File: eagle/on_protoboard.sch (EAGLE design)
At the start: 15 parts, among them IC2 7812T, K1 G6AK-434P

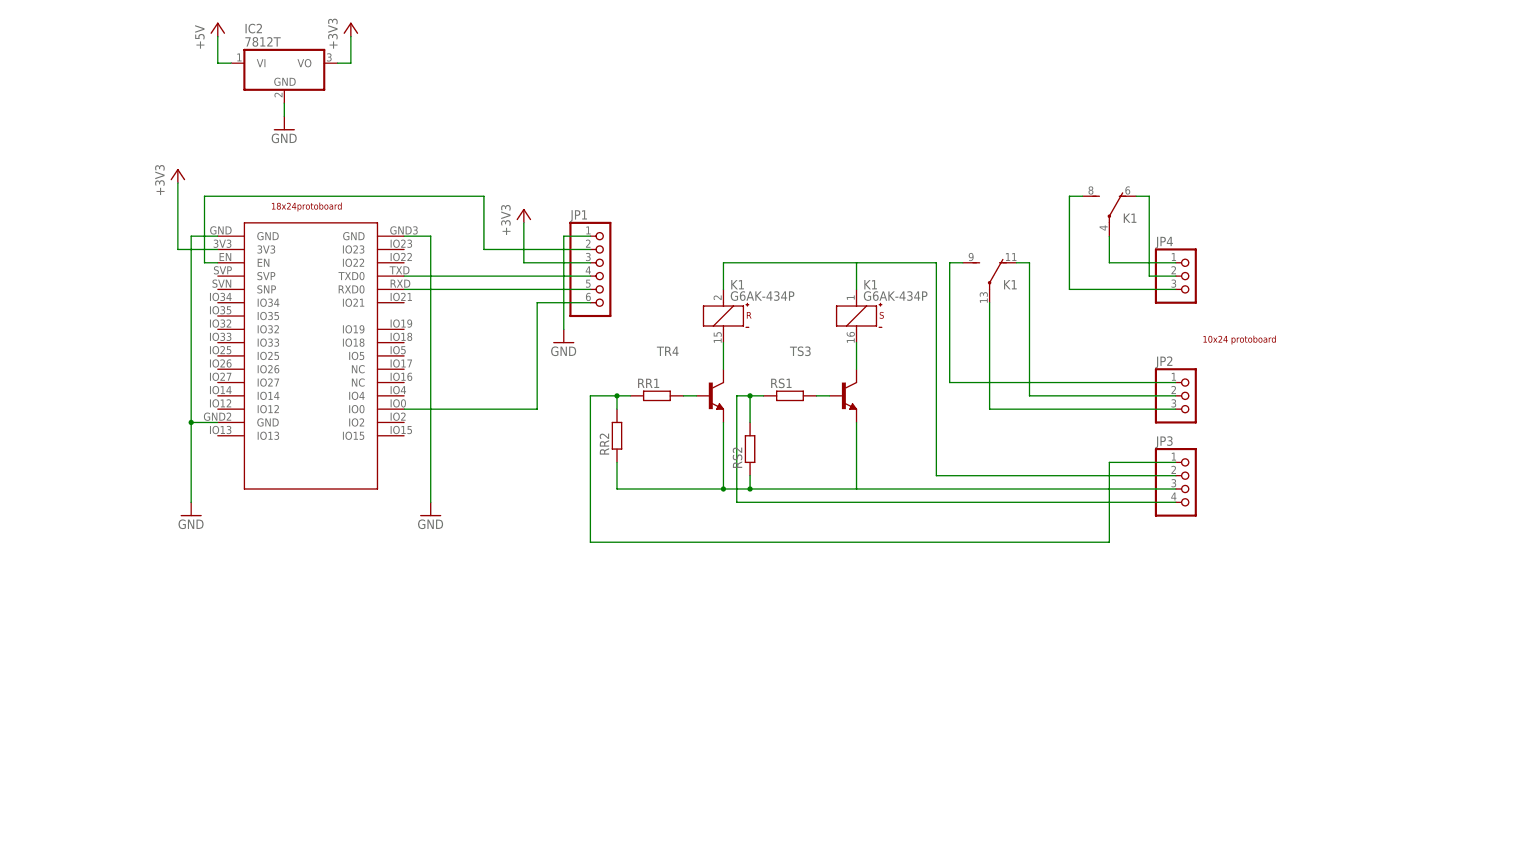
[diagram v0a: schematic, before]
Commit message: Add digital pulse output device
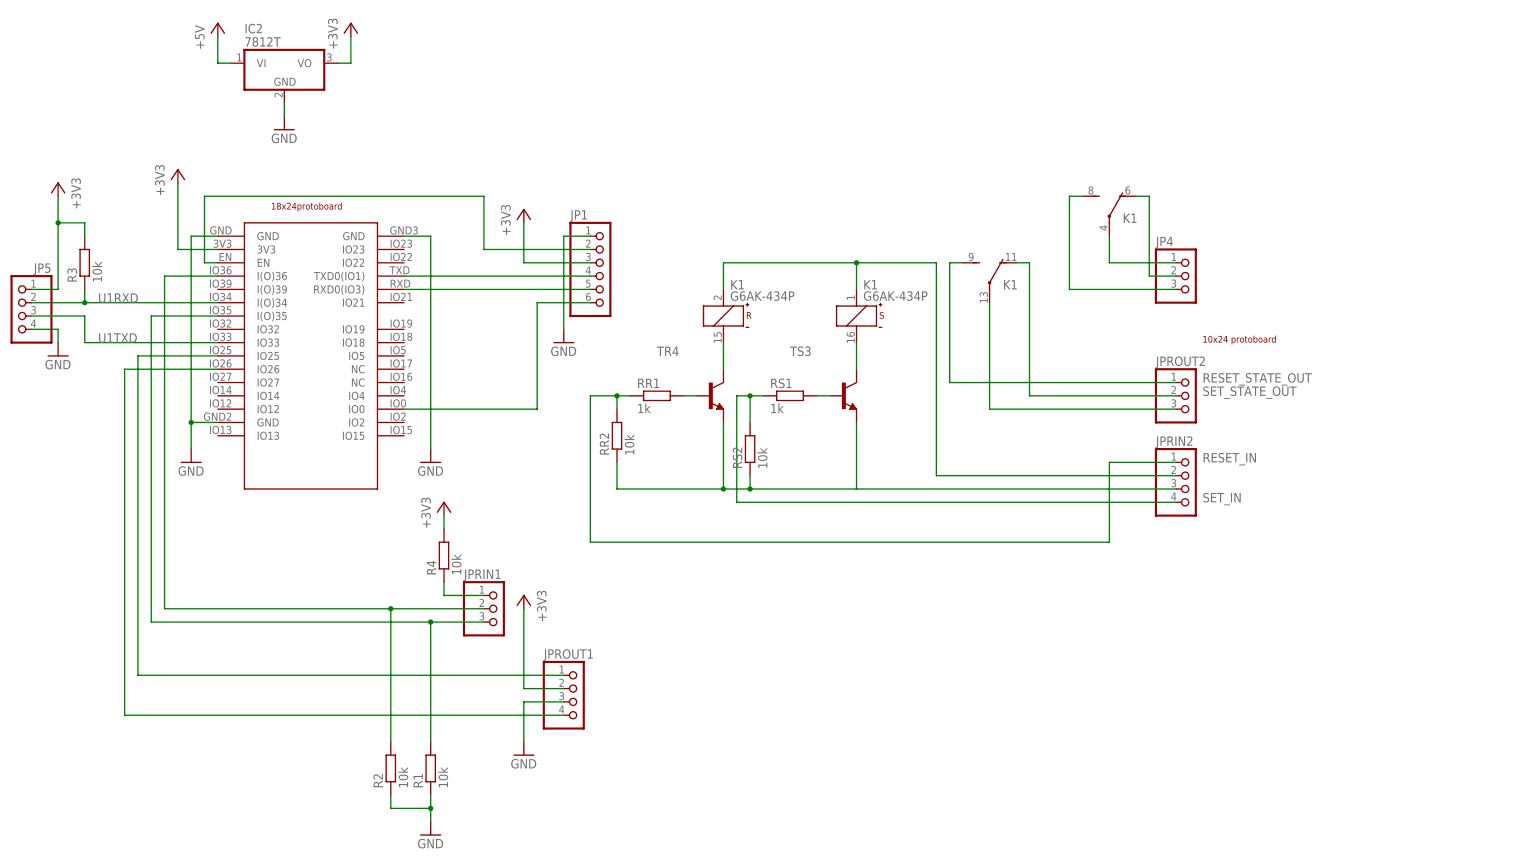
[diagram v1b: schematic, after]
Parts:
- added JP5, JPROUT1: (no value), pinhead:PINHD-1X4
- added JPRIN1: (no value), pinhead:PINHD-1X3
- added R1, R2, R3, R4: 10k, rcl:R-EU_R0603
- RR1, RS1: value (none) -> 1k
- RR2, RS2: value (none) -> 10k
- renumbered JP2 to JPROUT2, JP3 to JPRIN2
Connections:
- net N$12 renamed SET_STATE_OUT
- net N$13 renamed RESET_STATE_OUT
- net N$14 renamed SET_IN
- net N$17 renamed RESET_IN
- new net N$18: ESP-32S-ADAPTER-PCB1.I(O)35, JPRIN1.3, R1.2
- new net N$20: ESP-32S-ADAPTER-PCB1.I(O)36, JPRIN1.2, R2.2
- new net N$22: JPRIN1.1, R4.1
- new net N$23: ESP-32S-ADAPTER-PCB1.IO25, JPROUT1.1
- new net N$24: ESP-32S-ADAPTER-PCB1.IO26, JPROUT1.4
- new net U1RXD: ESP-32S-ADAPTER-PCB1.I(O)34, JP5.2, R3.1
- new net U1TXD: ESP-32S-ADAPTER-PCB1.IO33, JP5.3
- net +3V3: now also JP5.1, JPROUT1.2, R3.2, R4.2
- net GND: now also JP5.4, JPROUT1.3, R1.1, R2.1
- net N$3: now also ESP-32S-ADAPTER-PCB1.TXD0(IO1); no longer ESP-32S-ADAPTER-PCB1.TXD0
- net N$4: now also ESP-32S-ADAPTER-PCB1.RXD0(IO3); no longer ESP-32S-ADAPTER-PCB1.RXD0

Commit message: fix rf433
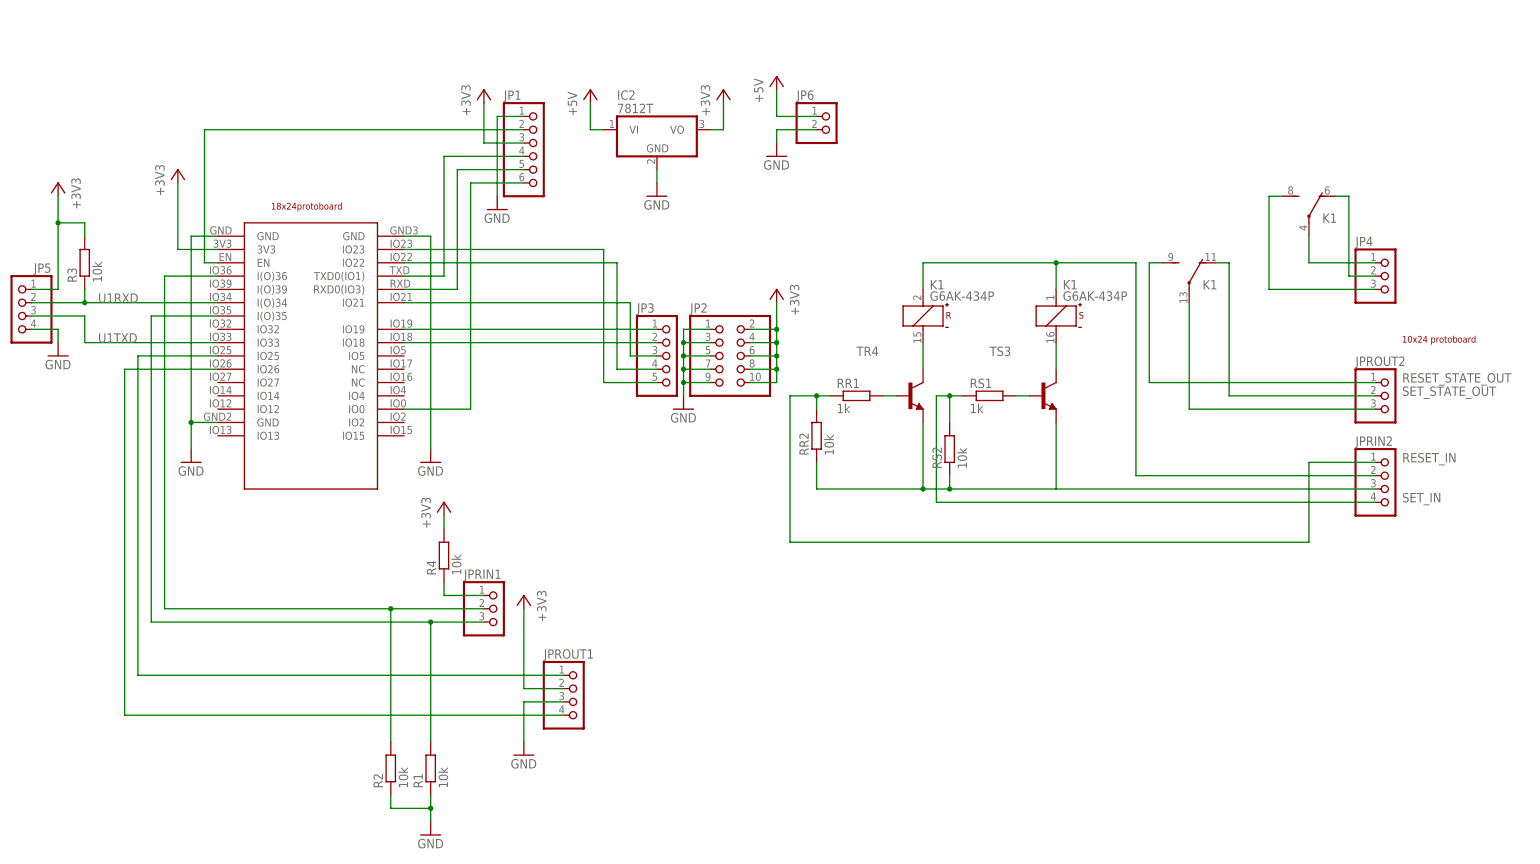
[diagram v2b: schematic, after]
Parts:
- added JP2: (no value), pinhead:PINHD-2X5
- added JP3: (no value), pinhead:PINHD-1X5
- added JP6: (no value), pinhead:PINHD-1X2
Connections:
- new net N$12: ESP-32S-ADAPTER-PCB1.IO19, JP3.1
- new net N$13: ESP-32S-ADAPTER-PCB1.IO18, JP3.2
- new net N$14: ESP-32S-ADAPTER-PCB1.IO21, JP3.3
- new net N$17: ESP-32S-ADAPTER-PCB1.IO22, JP3.4
- new net N$21: ESP-32S-ADAPTER-PCB1.IO23, JP3.5
- net +3V3: now also JP2.10, JP2.2, JP2.4, JP2.6, JP2.8
- net +5V: now also JP6.1
- net GND: now also JP2.1, JP2.3, JP2.5, JP2.7, JP2.9, JP6.2
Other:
- moved on the sheet: IC2, JP1, JP4, JPRIN2, JPROUT2, K1, RR1, RR2, RS1, RS2, TR4, TS3
